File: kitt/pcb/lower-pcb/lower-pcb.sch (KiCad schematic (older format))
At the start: 55 parts, among them J1 Screw_Terminal_01x02, Q1 NDP6020P, Q2 NDP6020P, Q3 NDP6020P, U6 TLC5940NT, U7 TLC5940NT, U8 TLC5940NT, U9 TLC5940NT

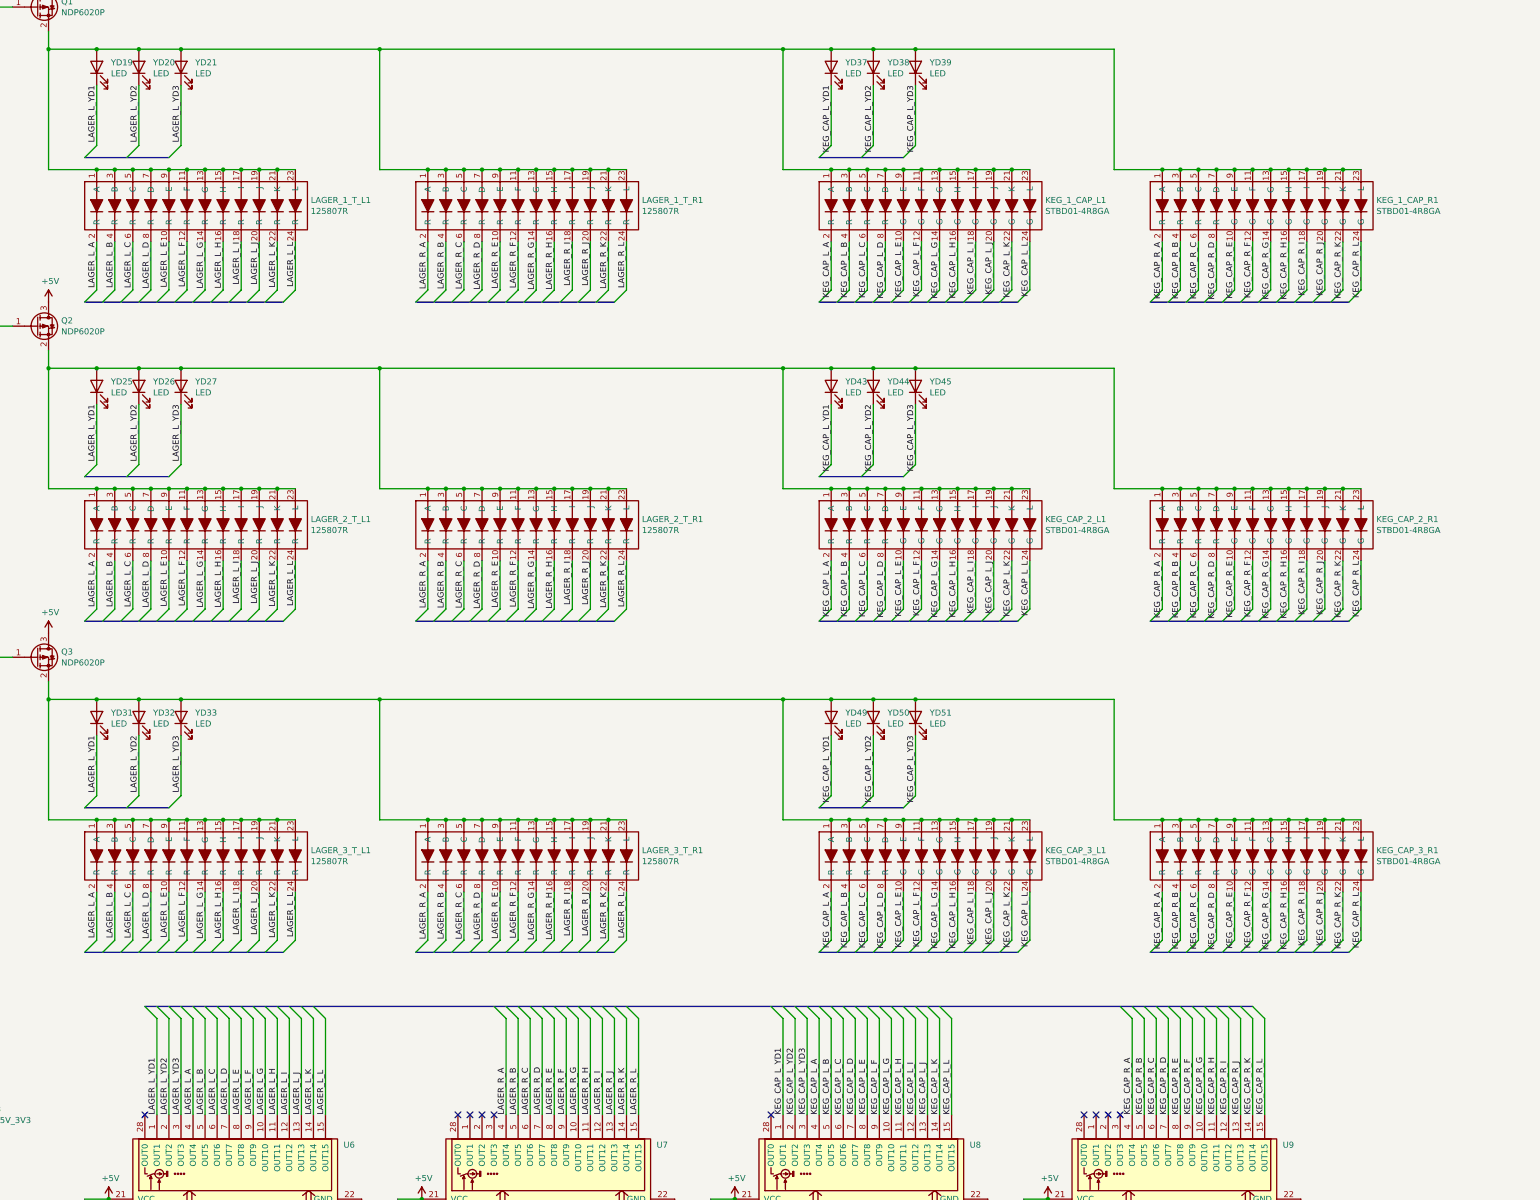
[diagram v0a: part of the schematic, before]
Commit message: fixed red and green bars
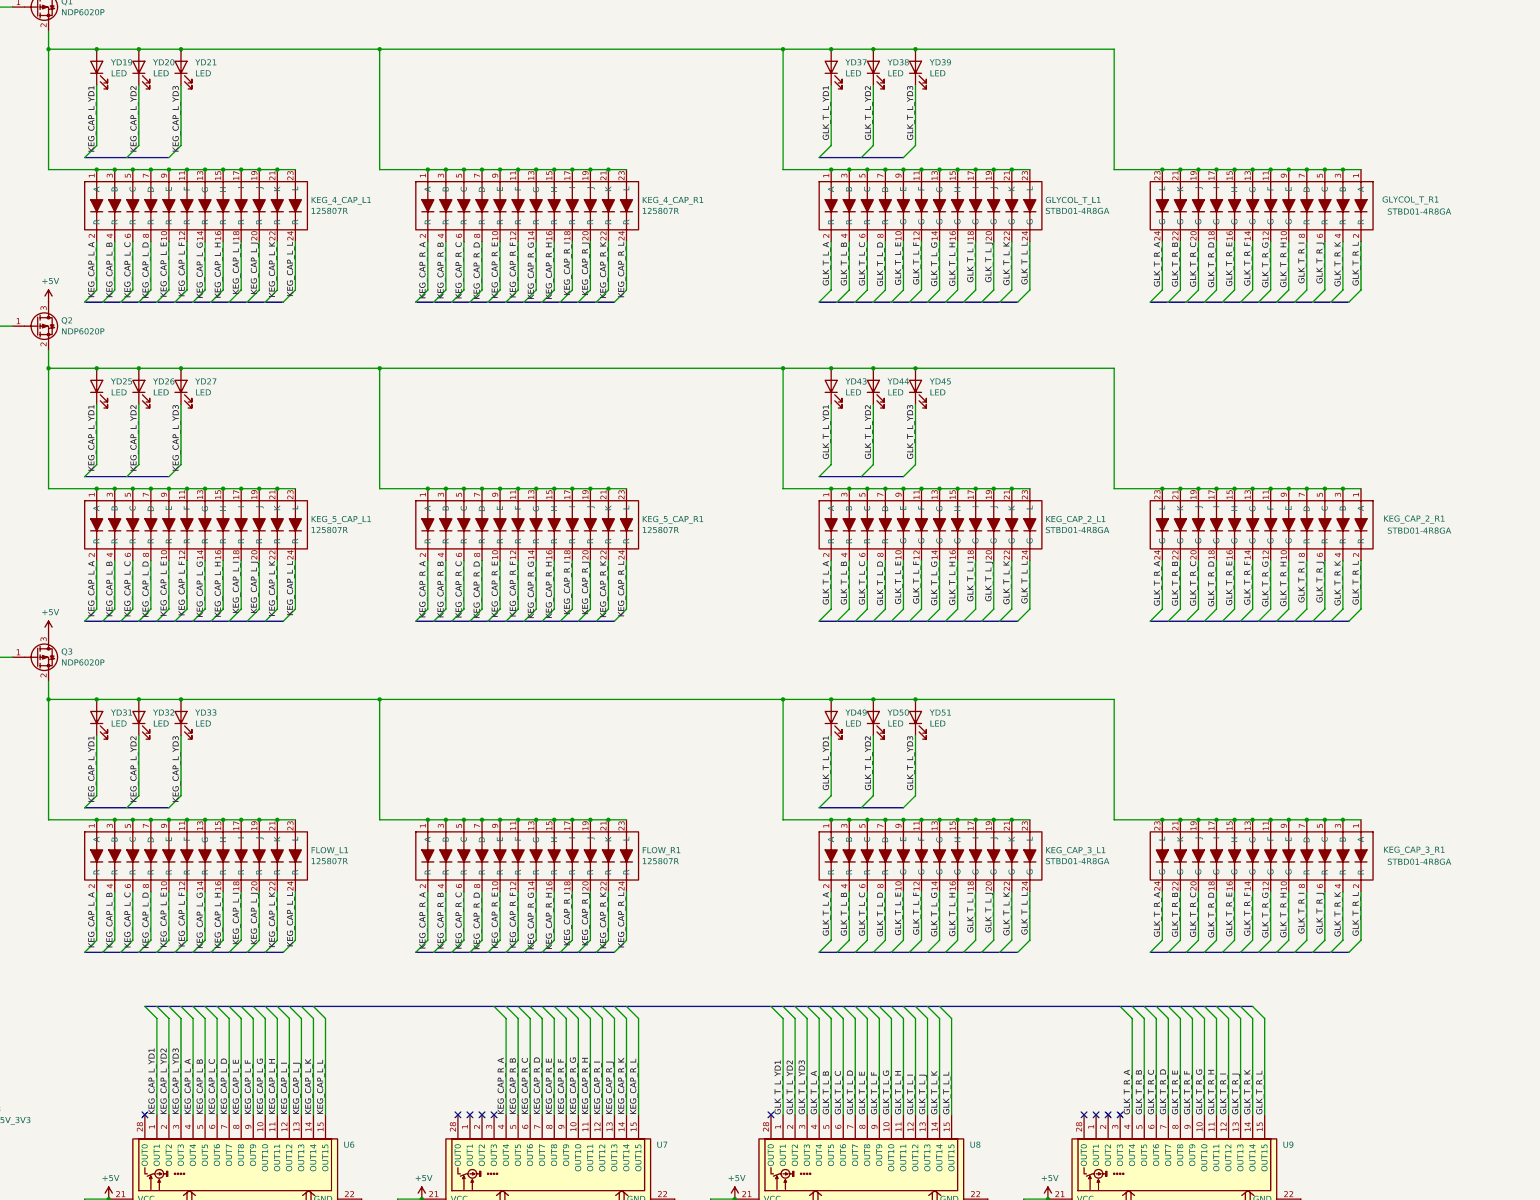
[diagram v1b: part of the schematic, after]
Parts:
- renumbered LAGER_3_T_L1 to FLOW_L1, LAGER_3_T_R1 to FLOW_R1, KEG_1_CAP_L1 to GLYCOL_T_L1, KEG_1_CAP_R1 to GLYCOL_T_R1, LAGER_1_T_L1 to KEG_4_CAP_L1, LAGER_1_T_R1 to KEG_4_CAP_R1, LAGER_2_T_L1 to KEG_5_CAP_L1, LAGER_2_T_R1 to KEG_5_CAP_R1
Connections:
- net LAGER_L_A is gone; now on net KEG_CAP_L_A: FLOW_L1.2 (R), KEG_4_CAP_L1.2 (R), KEG_5_CAP_L1.2 (R), U6.4 (OUT4)
- net LAGER_L_B is gone; now on net KEG_CAP_L_B: FLOW_L1.4 (R), KEG_4_CAP_L1.4 (R), KEG_5_CAP_L1.4 (R), U6.5 (OUT5)
- net LAGER_L_C is gone; now on net KEG_CAP_L_C: FLOW_L1.6 (R), KEG_4_CAP_L1.6 (R), KEG_5_CAP_L1.6 (R), U6.6 (OUT6)
- net LAGER_L_D is gone; now on net KEG_CAP_L_D: FLOW_L1.8 (R), KEG_4_CAP_L1.8 (R), KEG_5_CAP_L1.8 (R), U6.7 (OUT7)
- net LAGER_L_E is gone; now on net KEG_CAP_L_E: FLOW_L1.10 (R), KEG_4_CAP_L1.10 (R), KEG_5_CAP_L1.10 (R), U6.8 (OUT8)
- net LAGER_L_F is gone; now on net KEG_CAP_L_F: FLOW_L1.12 (R), KEG_4_CAP_L1.12 (R), KEG_5_CAP_L1.12 (R), U6.9 (OUT9)
- net LAGER_L_G is gone; now on net KEG_CAP_L_G: FLOW_L1.14 (R), KEG_4_CAP_L1.14 (R), KEG_5_CAP_L1.14 (R), U6.10 (OUT10)
- net LAGER_L_H is gone; now on net KEG_CAP_L_H: FLOW_L1.16 (R), KEG_4_CAP_L1.16 (R), KEG_5_CAP_L1.16 (R), U6.11 (OUT11)
- net LAGER_L_I is gone; now on net KEG_CAP_L_I: FLOW_L1.18 (R), KEG_4_CAP_L1.18 (R), KEG_5_CAP_L1.18 (R), U6.12 (OUT12)
- net LAGER_L_J is gone; now on net KEG_CAP_L_J: FLOW_L1.20 (R), KEG_4_CAP_L1.20 (R), KEG_5_CAP_L1.20 (R), U6.13 (OUT13)
- net LAGER_L_K is gone; now on net KEG_CAP_L_K: FLOW_L1.22 (R), KEG_4_CAP_L1.22 (R), KEG_5_CAP_L1.22 (R), U6.14 (OUT14)
- net LAGER_L_L is gone; now on net KEG_CAP_L_L: FLOW_L1.24 (R), KEG_4_CAP_L1.24 (R), KEG_5_CAP_L1.24 (R), U6.15 (OUT15)
- net LAGER_L_YD1 is gone; now on net KEG_CAP_L_YD1: U6.1 (OUT1), YD19.1 (K), YD25.1 (K), YD31.1 (K)
- net LAGER_L_YD2 is gone; now on net KEG_CAP_L_YD2: U6.2 (OUT2), YD20.1 (K), YD26.1 (K), YD32.1 (K)
- net LAGER_L_YD3 is gone; now on net KEG_CAP_L_YD3: U6.3 (OUT3), YD21.1 (K), YD27.1 (K), YD33.1 (K)
- net LAGER_R_A is gone; now on net KEG_CAP_R_A: FLOW_R1.2 (R), KEG_4_CAP_R1.2 (R), KEG_5_CAP_R1.2 (R), U7.4 (OUT4)
- net LAGER_R_B is gone; now on net KEG_CAP_R_B: FLOW_R1.4 (R), KEG_4_CAP_R1.4 (R), KEG_5_CAP_R1.4 (R), U7.5 (OUT5)
- net LAGER_R_C is gone; now on net KEG_CAP_R_C: FLOW_R1.6 (R), KEG_4_CAP_R1.6 (R), KEG_5_CAP_R1.6 (R), U7.6 (OUT6)
- net LAGER_R_D is gone; now on net KEG_CAP_R_D: FLOW_R1.8 (R), KEG_4_CAP_R1.8 (R), KEG_5_CAP_R1.8 (R), U7.7 (OUT7)
- net LAGER_R_E is gone; now on net KEG_CAP_R_E: FLOW_R1.10 (R), KEG_4_CAP_R1.10 (R), KEG_5_CAP_R1.10 (R), U7.8 (OUT8)
- net LAGER_R_F is gone; now on net KEG_CAP_R_F: FLOW_R1.12 (R), KEG_4_CAP_R1.12 (R), KEG_5_CAP_R1.12 (R), U7.9 (OUT9)
- net LAGER_R_G is gone; now on net KEG_CAP_R_G: FLOW_R1.14 (R), KEG_4_CAP_R1.14 (R), KEG_5_CAP_R1.14 (R), U7.10 (OUT10)
- net LAGER_R_H is gone; now on net KEG_CAP_R_H: FLOW_R1.16 (R), KEG_4_CAP_R1.16 (R), KEG_5_CAP_R1.16 (R), U7.11 (OUT11)
- net LAGER_R_I is gone; now on net KEG_CAP_R_I: FLOW_R1.18 (R), KEG_4_CAP_R1.18 (R), KEG_5_CAP_R1.18 (R), U7.12 (OUT12)
- net LAGER_R_J is gone; now on net KEG_CAP_R_J: FLOW_R1.20 (R), KEG_4_CAP_R1.20 (R), KEG_5_CAP_R1.20 (R), U7.13 (OUT13)
- net LAGER_R_K is gone; now on net KEG_CAP_R_K: FLOW_R1.22 (R), KEG_4_CAP_R1.22 (R), KEG_5_CAP_R1.22 (R), U7.14 (OUT14)
- net LAGER_R_L is gone; now on net KEG_CAP_R_L: FLOW_R1.24 (R), KEG_4_CAP_R1.24 (R), KEG_5_CAP_R1.24 (R), U7.15 (OUT15)
- net KEG_CAP_L_A: no longer GLYCOL_T_L1.2 (R), KEG_CAP_2_L1.2 (R), KEG_CAP_3_L1.2 (R), U8.4 (OUT4)
- net KEG_CAP_L_B: no longer GLYCOL_T_L1.4 (R), KEG_CAP_2_L1.4 (R), KEG_CAP_3_L1.4 (R), U8.5 (OUT5)
- net KEG_CAP_L_C: no longer GLYCOL_T_L1.6 (R), KEG_CAP_2_L1.6 (R), KEG_CAP_3_L1.6 (R), U8.6 (OUT6)
- net KEG_CAP_L_D: no longer GLYCOL_T_L1.8 (R), KEG_CAP_2_L1.8 (R), KEG_CAP_3_L1.8 (R), U8.7 (OUT7)
- net KEG_CAP_L_E: no longer GLYCOL_T_L1.10 (G), KEG_CAP_2_L1.10 (G), KEG_CAP_3_L1.10 (G), U8.8 (OUT8)
- net KEG_CAP_L_F: no longer GLYCOL_T_L1.12 (G), KEG_CAP_2_L1.12 (G), KEG_CAP_3_L1.12 (G), U8.9 (OUT9)
- net KEG_CAP_L_G: no longer GLYCOL_T_L1.14 (G), KEG_CAP_2_L1.14 (G), KEG_CAP_3_L1.14 (G), U8.10 (OUT10)
- net KEG_CAP_L_H: no longer GLYCOL_T_L1.16 (G), KEG_CAP_2_L1.16 (G), KEG_CAP_3_L1.16 (G), U8.11 (OUT11)
- net KEG_CAP_L_I: no longer GLYCOL_T_L1.18 (G), KEG_CAP_2_L1.18 (G), KEG_CAP_3_L1.18 (G), U8.12 (OUT12)
- net KEG_CAP_L_J: no longer GLYCOL_T_L1.20 (G), KEG_CAP_2_L1.20 (G), KEG_CAP_3_L1.20 (G), U8.13 (OUT13)
- net KEG_CAP_L_K: no longer GLYCOL_T_L1.22 (G), KEG_CAP_2_L1.22 (G), KEG_CAP_3_L1.22 (G), U8.14 (OUT14)
- net KEG_CAP_L_L: no longer GLYCOL_T_L1.24 (G), KEG_CAP_2_L1.24 (G), KEG_CAP_3_L1.24 (G), U8.15 (OUT15)
- net KEG_CAP_L_YD1: no longer U8.1 (OUT1), YD37.1 (K), YD43.1 (K), YD49.1 (K)
- net KEG_CAP_L_YD2: no longer U8.2 (OUT2), YD38.1 (K), YD44.1 (K), YD50.1 (K)
- net KEG_CAP_L_YD3: no longer U8.3 (OUT3), YD39.1 (K), YD45.1 (K), YD51.1 (K)
- net KEG_CAP_R_A: no longer GLYCOL_T_R1.2 (R), KEG_CAP_2_R1.2 (R), KEG_CAP_3_R1.2 (R), U9.4 (OUT4)
- net KEG_CAP_R_B: no longer GLYCOL_T_R1.4 (R), KEG_CAP_2_R1.4 (R), KEG_CAP_3_R1.4 (R), U9.5 (OUT5)
- net KEG_CAP_R_C: no longer GLYCOL_T_R1.6 (R), KEG_CAP_2_R1.6 (R), KEG_CAP_3_R1.6 (R), U9.6 (OUT6)
- net KEG_CAP_R_D: no longer GLYCOL_T_R1.8 (R), KEG_CAP_2_R1.8 (R), KEG_CAP_3_R1.8 (R), U9.7 (OUT7)
- net KEG_CAP_R_E: no longer GLYCOL_T_R1.10 (G), KEG_CAP_2_R1.10 (G), KEG_CAP_3_R1.10 (G), U9.8 (OUT8)
- net KEG_CAP_R_F: no longer GLYCOL_T_R1.12 (G), KEG_CAP_2_R1.12 (G), KEG_CAP_3_R1.12 (G), U9.9 (OUT9)
- net KEG_CAP_R_G: no longer GLYCOL_T_R1.14 (G), KEG_CAP_2_R1.14 (G), KEG_CAP_3_R1.14 (G), U9.10 (OUT10)
- net KEG_CAP_R_H: no longer GLYCOL_T_R1.16 (G), KEG_CAP_2_R1.16 (G), KEG_CAP_3_R1.16 (G), U9.11 (OUT11)
- net KEG_CAP_R_I: no longer GLYCOL_T_R1.18 (G), KEG_CAP_2_R1.18 (G), KEG_CAP_3_R1.18 (G), U9.12 (OUT12)
- net KEG_CAP_R_J: no longer GLYCOL_T_R1.20 (G), KEG_CAP_2_R1.20 (G), KEG_CAP_3_R1.20 (G), U9.13 (OUT13)
- net KEG_CAP_R_K: no longer GLYCOL_T_R1.22 (G), KEG_CAP_2_R1.22 (G), KEG_CAP_3_R1.22 (G), U9.14 (OUT14)
- net KEG_CAP_R_L: no longer GLYCOL_T_R1.24 (G), KEG_CAP_2_R1.24 (G), KEG_CAP_3_R1.24 (G), U9.15 (OUT15)
- new net GLK_T_L_A: GLYCOL_T_L1.2 (R), KEG_CAP_2_L1.2 (R), KEG_CAP_3_L1.2 (R), U8.4 (OUT4)
- new net GLK_T_L_B: GLYCOL_T_L1.4 (R), KEG_CAP_2_L1.4 (R), KEG_CAP_3_L1.4 (R), U8.5 (OUT5)
- new net GLK_T_L_C: GLYCOL_T_L1.6 (R), KEG_CAP_2_L1.6 (R), KEG_CAP_3_L1.6 (R), U8.6 (OUT6)
- new net GLK_T_L_D: GLYCOL_T_L1.8 (R), KEG_CAP_2_L1.8 (R), KEG_CAP_3_L1.8 (R), U8.7 (OUT7)
- new net GLK_T_L_E: GLYCOL_T_L1.10 (G), KEG_CAP_2_L1.10 (G), KEG_CAP_3_L1.10 (G), U8.8 (OUT8)
- new net GLK_T_L_F: GLYCOL_T_L1.12 (G), KEG_CAP_2_L1.12 (G), KEG_CAP_3_L1.12 (G), U8.9 (OUT9)
- new net GLK_T_L_G: GLYCOL_T_L1.14 (G), KEG_CAP_2_L1.14 (G), KEG_CAP_3_L1.14 (G), U8.10 (OUT10)
- new net GLK_T_L_H: GLYCOL_T_L1.16 (G), KEG_CAP_2_L1.16 (G), KEG_CAP_3_L1.16 (G), U8.11 (OUT11)
- new net GLK_T_L_I: GLYCOL_T_L1.18 (G), KEG_CAP_2_L1.18 (G), KEG_CAP_3_L1.18 (G), U8.12 (OUT12)
- new net GLK_T_L_J: GLYCOL_T_L1.20 (G), KEG_CAP_2_L1.20 (G), KEG_CAP_3_L1.20 (G), U8.13 (OUT13)
- new net GLK_T_L_K: GLYCOL_T_L1.22 (G), KEG_CAP_2_L1.22 (G), KEG_CAP_3_L1.22 (G), U8.14 (OUT14)
- new net GLK_T_L_L: GLYCOL_T_L1.24 (G), KEG_CAP_2_L1.24 (G), KEG_CAP_3_L1.24 (G), U8.15 (OUT15)
- new net GLK_T_L_YD1: U8.1 (OUT1), YD37.1 (K), YD43.1 (K), YD49.1 (K)
- new net GLK_T_L_YD2: U8.2 (OUT2), YD38.1 (K), YD44.1 (K), YD50.1 (K)
- new net GLK_T_L_YD3: U8.3 (OUT3), YD39.1 (K), YD45.1 (K), YD51.1 (K)
- new net GLK_T_R_A: GLYCOL_T_R1.24 (G), KEG_CAP_2_R1.24 (G), KEG_CAP_3_R1.24 (G), U9.4 (OUT4)
- new net GLK_T_R_B: GLYCOL_T_R1.22 (G), KEG_CAP_2_R1.22 (G), KEG_CAP_3_R1.22 (G), U9.5 (OUT5)
- new net GLK_T_R_C: GLYCOL_T_R1.20 (G), KEG_CAP_2_R1.20 (G), KEG_CAP_3_R1.20 (G), U9.6 (OUT6)
- new net GLK_T_R_D: GLYCOL_T_R1.18 (G), KEG_CAP_2_R1.18 (G), KEG_CAP_3_R1.18 (G), U9.7 (OUT7)
- new net GLK_T_R_E: GLYCOL_T_R1.16 (G), KEG_CAP_2_R1.16 (G), KEG_CAP_3_R1.16 (G), U9.8 (OUT8)
- new net GLK_T_R_F: GLYCOL_T_R1.14 (G), KEG_CAP_2_R1.14 (G), KEG_CAP_3_R1.14 (G), U9.9 (OUT9)
- new net GLK_T_R_G: GLYCOL_T_R1.12 (G), KEG_CAP_2_R1.12 (G), KEG_CAP_3_R1.12 (G), U9.10 (OUT10)
- new net GLK_T_R_H: GLYCOL_T_R1.10 (G), KEG_CAP_2_R1.10 (G), KEG_CAP_3_R1.10 (G), U9.11 (OUT11)
- new net GLK_T_R_I: GLYCOL_T_R1.8 (R), KEG_CAP_2_R1.8 (R), KEG_CAP_3_R1.8 (R), U9.12 (OUT12)
- new net GLK_T_R_J: GLYCOL_T_R1.6 (R), KEG_CAP_2_R1.6 (R), KEG_CAP_3_R1.6 (R), U9.13 (OUT13)
- new net GLK_T_R_K: GLYCOL_T_R1.4 (R), KEG_CAP_2_R1.4 (R), KEG_CAP_3_R1.4 (R), U9.14 (OUT14)
- new net GLK_T_R_L: GLYCOL_T_R1.2 (R), KEG_CAP_2_R1.2 (R), KEG_CAP_3_R1.2 (R), U9.15 (OUT15)

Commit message: sed to get flangeless led
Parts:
- YD19, YD20, YD21, YD25, YD26, YD27, YD31, YD32, YD33, YD37, YD38, YD39, YD43, YD44, YD45, YD49, YD50, YD51: footprint (none) -> KITT-Footpads:Flangeless_LED
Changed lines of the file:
@@
 F 0 "YD33" V 4239 7682 50  0000 R CNN
 F 1 "LED" V 4148 7682 50  0000 R CNN
-F 2 "" H 4200 7800 50  0001 C CNN
+F 2 "KITT-Footpads:Flangeless_LED" H 4200 7800 50  0001 C CNN
 F 3 "~" H 4200 7800 50  0001 C CNN
 	1    4200 7800
@@
 F 0 "YD32" V 3889 7682 50  0000 R CNN
 F 1 "LED" V 3798 7682 50  0000 R CNN
-F 2 "" H 3850 7800 50  0001 C CNN
+F 2 "KITT-Footpads:Flangeless_LED" H 3850 7800 50  0001 C CNN
 F 3 "~" H 3850 7800 50  0001 C CNN
 	1    3850 7800
@@
 F 0 "YD31" V 3539 7682 50  0000 R CNN
 F 1 "LED" V 3448 7682 50  0000 R CNN
-F 2 "" H 3500 7800 50  0001 C CNN
+F 2 "KITT-Footpads:Flangeless_LED" H 3500 7800 50  0001 C CNN
 F 3 "~" H 3500 7800 50  0001 C CNN
 	1    3500 7800
@@
 F 0 "YD27" V 4239 4932 50  0000 R CNN
 F 1 "LED" V 4148 4932 50  0000 R CNN
-F 2 "" H 4200 5050 50  0001 C CNN
+F 2 "KITT-Footpads:Flangeless_LED" H 4200 5050 50  0001 C CNN
 F 3 "~" H 4200 5050 50  0001 C CNN
 	1    4200 5050
@@
 F 0 "YD26" V 3889 4932 50  0000 R CNN
 F 1 "LED" V 3798 4932 50  0000 R CNN
-F 2 "" H 3850 5050 50  0001 C CNN
+F 2 "KITT-Footpads:Flangeless_LED" H 3850 5050 50  0001 C CNN
 F 3 "~" H 3850 5050 50  0001 C CNN
 	1    3850 5050
@@
 F 0 "YD25" V 3539 4932 50  0000 R CNN
 F 1 "LED" V 3448 4932 50  0000 R CNN
-F 2 "" H 3500 5050 50  0001 C CNN
+F 2 "KITT-Footpads:Flangeless_LED" H 3500 5050 50  0001 C CNN
 F 3 "~" H 3500 5050 50  0001 C CNN
 	1    3500 5050
@@
 F 0 "YD21" V 4239 2282 50  0000 R CNN
 F 1 "LED" V 4148 2282 50  0000 R CNN
-F 2 "" H 4200 2400 50  0001 C CNN
+F 2 "KITT-Footpads:Flangeless_LED" H 4200 2400 50  0001 C CNN
 F 3 "~" H 4200 2400 50  0001 C CNN
 	1    4200 2400
@@
 F 0 "YD20" V 3889 2282 50  0000 R CNN
 F 1 "LED" V 3798 2282 50  0000 R CNN
-F 2 "" H 3850 2400 50  0001 C CNN
+F 2 "KITT-Footpads:Flangeless_LED" H 3850 2400 50  0001 C CNN
 F 3 "~" H 3850 2400 50  0001 C CNN
 	1    3850 2400
@@
 F 0 "YD19" V 3539 2282 50  0000 R CNN
 F 1 "LED" V 3448 2282 50  0000 R CNN
-F 2 "" H 3500 2400 50  0001 C CNN
+F 2 "KITT-Footpads:Flangeless_LED" H 3500 2400 50  0001 C CNN
 F 3 "~" H 3500 2400 50  0001 C CNN
 	1    3500 2400
@@
 F 0 "YD37" V 9639 2282 50  0000 R CNN
 F 1 "LED" V 9548 2282 50  0000 R CNN
-F 2 "" H 9600 2400 50  0001 C CNN
+F 2 "KITT-Footpads:Flangeless_LED" H 9600 2400 50  0001 C CNN
 F 3 "~" H 9600 2400 50  0001 C CNN
 	1    9600 2400
@@
 F 0 "YD38" V 9989 2282 50  0000 R CNN
 F 1 "LED" V 9898 2282 50  0000 R CNN
-F 2 "" H 9950 2400 50  0001 C CNN
+F 2 "KITT-Footpads:Flangeless_LED" H 9950 2400 50  0001 C CNN
 F 3 "~" H 9950 2400 50  0001 C CNN
 	1    9950 2400
@@
 F 0 "YD39" V 10339 2282 50  0000 R CNN
 F 1 "LED" V 10248 2282 50  0000 R CNN
-F 2 "" H 10300 2400 50  0001 C CNN
+F 2 "KITT-Footpads:Flangeless_LED" H 10300 2400 50  0001 C CNN
 F 3 "~" H 10300 2400 50  0001 C CNN
 	1    10300 2400
@@
 F 0 "YD43" V 9639 4932 50  0000 R CNN
 F 1 "LED" V 9548 4932 50  0000 R CNN
-F 2 "" H 9600 5050 50  0001 C CNN
+F 2 "KITT-Footpads:Flangeless_LED" H 9600 5050 50  0001 C CNN
 F 3 "~" H 9600 5050 50  0001 C CNN
 	1    9600 5050
@@
 F 0 "YD44" V 9989 4932 50  0000 R CNN
 F 1 "LED" V 9898 4932 50  0000 R CNN
-F 2 "" H 9950 5050 50  0001 C CNN
+F 2 "KITT-Footpads:Flangeless_LED" H 9950 5050 50  0001 C CNN
 F 3 "~" H 9950 5050 50  0001 C CNN
 	1    9950 5050
@@
 F 0 "YD45" V 10339 4932 50  0000 R CNN
 F 1 "LED" V 10248 4932 50  0000 R CNN
-F 2 "" H 10300 5050 50  0001 C CNN
+F 2 "KITT-Footpads:Flangeless_LED" H 10300 5050 50  0001 C CNN
 F 3 "~" H 10300 5050 50  0001 C CNN
 	1    10300 5050
@@
 F 0 "YD49" V 9639 7682 50  0000 R CNN
 F 1 "LED" V 9548 7682 50  0000 R CNN
-F 2 "" H 9600 7800 50  0001 C CNN
+F 2 "KITT-Footpads:Flangeless_LED" H 9600 7800 50  0001 C CNN
 F 3 "~" H 9600 7800 50  0001 C CNN
 	1    9600 7800
@@
 F 0 "YD50" V 9989 7682 50  0000 R CNN
 F 1 "LED" V 9898 7682 50  0000 R CNN
-F 2 "" H 9950 7800 50  0001 C CNN
+F 2 "KITT-Footpads:Flangeless_LED" H 9950 7800 50  0001 C CNN
 F 3 "~" H 9950 7800 50  0001 C CNN
 	1    9950 7800
@@
 F 0 "YD51" V 10339 7682 50  0000 R CNN
 F 1 "LED" V 10248 7682 50  0000 R CNN
-F 2 "" H 10300 7800 50  0001 C CNN
+F 2 "KITT-Footpads:Flangeless_LED" H 10300 7800 50  0001 C CNN
 F 3 "~" H 10300 7800 50  0001 C CNN
 	1    10300 7800

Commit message: add 12 seg led footprints
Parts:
- FLOW_L1, FLOW_R1, GLYCOL_T_L1, GLYCOL_T_R1, KEG_4_CAP_L1, KEG_4_CAP_R1, KEG_5_CAP_L1, KEG_5_CAP_R1, KEG_CAP_2_L1, KEG_CAP_2_R1, KEG_CAP_3_L1, KEG_CAP_3_R1: footprint (none) -> KITT-Footpads:LED_12_Segment_2.0mm_24_pin
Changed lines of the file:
@@
 F 0 "KEG_CAP_2_L1" H 11378 6246 50  0000 L CNN
 F 1 "STBD01-4R8GA" H 11378 6155 50  0000 L CNN
-F 2 "" H 9600 6500 50  0001 C CNN
+F 2 "KITT-Footpads:LED_12_Segment_2.0mm_24_pin" H 9600 6500 50  0001 C CNN
 F 3 "" H 9600 6500 50  0001 C CNN
 	1    10550 6200
@@
 F 0 "KEG_CAP_2_R1" H 11400 6250 50  0000 L CNN
 F 1 "STBD01-4R8GA" H 11350 6150 50  0000 L CNN
-F 2 "" H 12100 6500 50  0001 C CNN
+F 2 "KITT-Footpads:LED_12_Segment_2.0mm_24_pin" H 12100 6500 50  0001 C CNN
 F 3 "" H 12100 6500 50  0001 C CNN
 	1    13050 6200
@@
 F 0 "KEG_CAP_3_L1" H 11378 8996 50  0000 L CNN
 F 1 "STBD01-4R8GA" H 11378 8905 50  0000 L CNN
-F 2 "" H 9600 9250 50  0001 C CNN
+F 2 "KITT-Footpads:LED_12_Segment_2.0mm_24_pin" H 9600 9250 50  0001 C CNN
 F 3 "" H 9600 9250 50  0001 C CNN
 	1    10550 8950
@@
 F 0 "KEG_4_CAP_L1" H 5278 3596 50  0000 L CNN
 F 1 "125807R" H 5278 3505 50  0000 L CNN
-F 2 "" H 3500 3850 50  0001 C CNN
+F 2 "KITT-Footpads:LED_12_Segment_2.0mm_24_pin" H 3500 3850 50  0001 C CNN
 F 3 "" H 3500 3850 50  0001 C CNN
 	1    4450 3550
@@
 F 0 "KEG_4_CAP_R1" H 8028 3596 50  0000 L CNN
 F 1 "125807R" H 8028 3505 50  0000 L CNN
-F 2 "" H 6250 3850 50  0001 C CNN
+F 2 "KITT-Footpads:LED_12_Segment_2.0mm_24_pin" H 6250 3850 50  0001 C CNN
 F 3 "" H 6250 3850 50  0001 C CNN
 	1    7200 3550
@@
 F 0 "KEG_5_CAP_L1" H 5278 6246 50  0000 L CNN
 F 1 "125807R" H 5278 6155 50  0000 L CNN
-F 2 "" H 3500 6500 50  0001 C CNN
+F 2 "KITT-Footpads:LED_12_Segment_2.0mm_24_pin" H 3500 6500 50  0001 C CNN
 F 3 "" H 3500 6500 50  0001 C CNN
 	1    4450 6200
@@
 F 0 "KEG_5_CAP_R1" H 8028 6246 50  0000 L CNN
 F 1 "125807R" H 8028 6155 50  0000 L CNN
-F 2 "" H 6250 6500 50  0001 C CNN
+F 2 "KITT-Footpads:LED_12_Segment_2.0mm_24_pin" H 6250 6500 50  0001 C CNN
 F 3 "" H 6250 6500 50  0001 C CNN
 	1    7200 6200
@@
 F 0 "FLOW_L1" H 5278 8996 50  0000 L CNN
 F 1 "125807R" H 5278 8905 50  0000 L CNN
-F 2 "" H 3500 9250 50  0001 C CNN
+F 2 "KITT-Footpads:LED_12_Segment_2.0mm_24_pin" H 3500 9250 50  0001 C CNN
 F 3 "" H 3500 9250 50  0001 C CNN
 	1    4450 8950
@@
 F 0 "FLOW_R1" H 8028 8996 50  0000 L CNN
 F 1 "125807R" H 8028 8905 50  0000 L CNN
-F 2 "" H 6250 9250 50  0001 C CNN
+F 2 "KITT-Footpads:LED_12_Segment_2.0mm_24_pin" H 6250 9250 50  0001 C CNN
 F 3 "" H 6250 9250 50  0001 C CNN
 	1    7200 8950
@@
 F 0 "GLYCOL_T_L1" H 11378 3596 50  0000 L CNN
 F 1 "STBD01-4R8GA" H 11378 3505 50  0000 L CNN
-F 2 "" H 9600 3850 50  0001 C CNN
+F 2 "KITT-Footpads:LED_12_Segment_2.0mm_24_pin" H 9600 3850 50  0001 C CNN
 F 3 "" H 9600 3850 50  0001 C CNN
 	1    10550 3550
@@
 F 0 "GLYCOL_T_R1" H 11450 3600 50  0000 L CNN
 F 1 "STBD01-4R8GA" H 11350 3500 50  0000 L CNN
-F 2 "" H 12100 3850 50  0001 C CNN
+F 2 "KITT-Footpads:LED_12_Segment_2.0mm_24_pin" H 12100 3850 50  0001 C CNN
 F 3 "" H 12100 3850 50  0001 C CNN
 	1    13050 3550
@@
 F 0 "KEG_CAP_3_R1" H 11400 9000 50  0000 L CNN
 F 1 "STBD01-4R8GA" H 11350 8900 50  0000 L CNN
-F 2 "" H 12100 9250 50  0001 C CNN
+F 2 "KITT-Footpads:LED_12_Segment_2.0mm_24_pin" H 12100 9250 50  0001 C CNN
 F 3 "" H 12100 9250 50  0001 C CNN
 	1    13050 8950

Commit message: added footpads
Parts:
- J1: footprint (none) -> KITT-Footpads:5mm_Screw_Terminal_01x02
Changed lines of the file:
@@
 F 0 "J1" H 7268 14717 50  0000 C CNN
 F 1 "Screw_Terminal_01x02" H 7268 14626 50  0000 C CNN
-F 2 "" H 7350 14500 50  0001 C CNN
+F 2 "KITT-Footpads:5mm_Screw_Terminal_01x02" H 7350 14500 50  0001 C CNN
 F 3 "~" H 7350 14500 50  0001 C CNN
 	1    7350 14500
@@
 Wire Wire Line
 	13700 8650 13850 8650
+Connection ~ 13850 8650
+Wire Wire Line
+	13850 8650 14000 8650
 Wire Bus Line
 	9500 8550 10200 8550
@@
 Wire Bus Line
 	3900 10200 13100 10200
-Connection ~ 13850 8650
-Wire Wire Line
-	13850 8650 14000 8650
 $EndSCHEMATC

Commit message: add footpad for logic level shifter
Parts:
- LVL3: footprint (none) -> KITT-Footpads:LVL_5V_3V3
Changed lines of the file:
@@
 F 0 "LVL3" V 2104 11488 50  0000 L CNN
 F 1 "LVL_5V_3V3" V 2195 11488 50  0000 L CNN
-F 2 "" H 2150 11100 50  0001 C CNN
+F 2 "KITT-Footpads:LVL_5V_3V3" H 2150 11100 50  0001 C CNN
 F 3 "" H 2150 11100 50  0001 C CNN
 	1    2150 11100
